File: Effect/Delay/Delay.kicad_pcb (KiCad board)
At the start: 2 copper layers, 32 x 75 mm, 23 parts, among them J1 Conn_01x04_Pin, J2 Conn_01x03_Pin, U1 PT2399

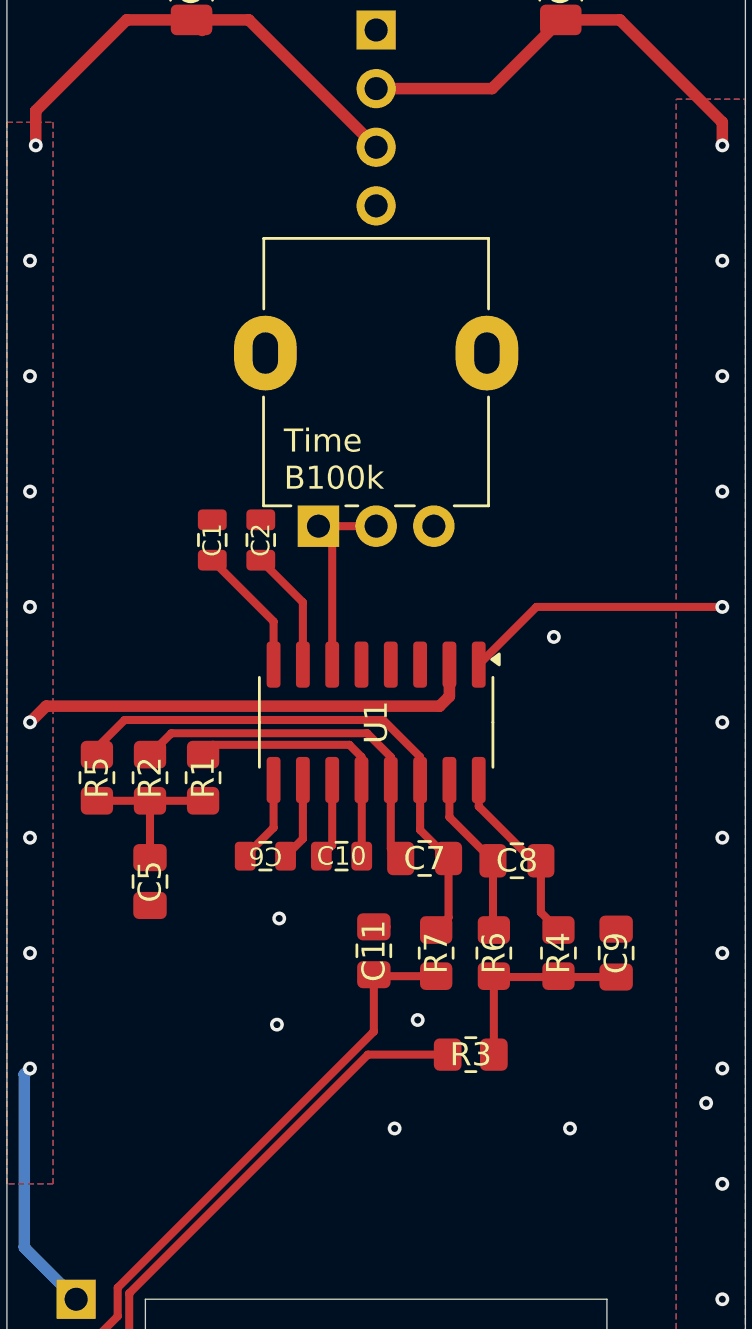
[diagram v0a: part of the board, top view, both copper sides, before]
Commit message: Do the manual ground stitching on delay board
Still don't have automated scripts, and I still like having something
that looks like ground stitching when prepping for fabrication.

Signed-off-by: Linus Torvalds <torvalds@linux-foundation.org>
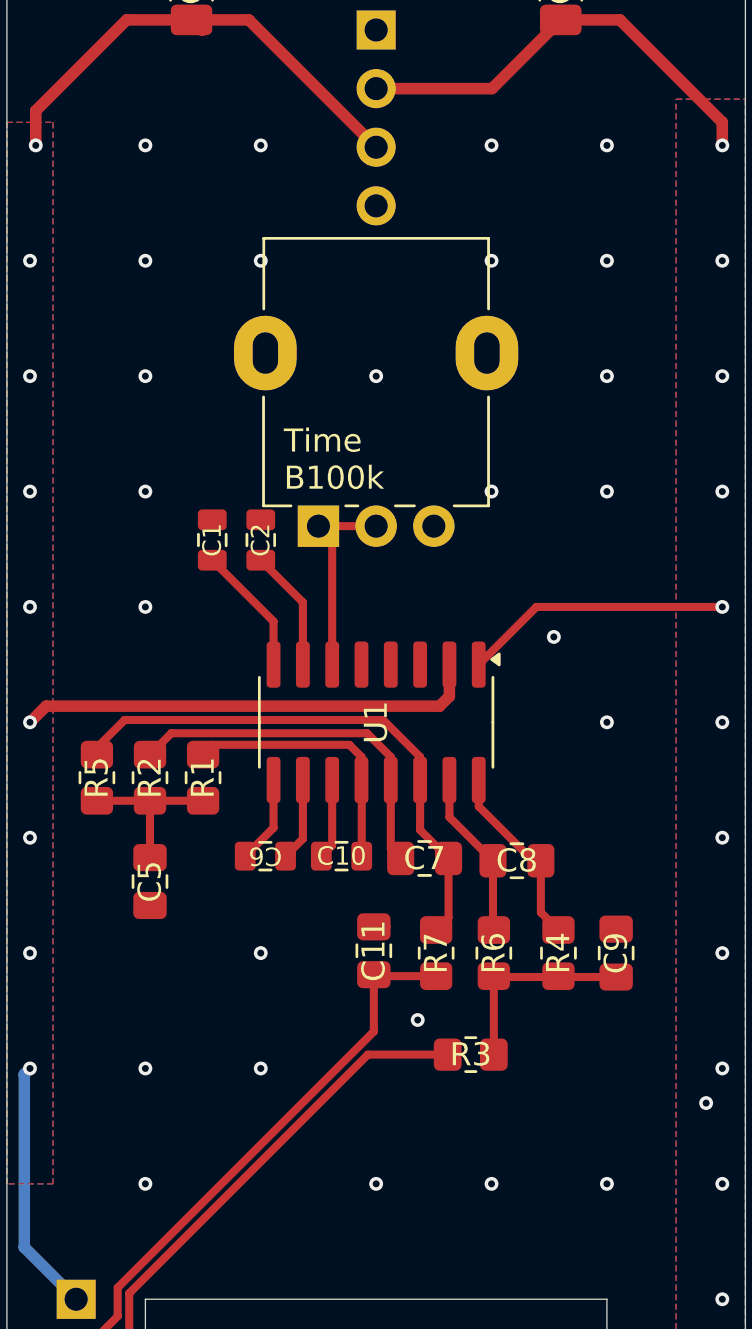
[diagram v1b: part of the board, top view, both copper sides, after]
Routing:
- net AGND: vias 11 -> 30
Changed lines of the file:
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@@
+	)
+	(via
+		(at 90 115)
+		(size 0.6)
+		(drill 0.3)
+		(layers "F.Cu" "B.Cu")
+		(free yes)
+		(net 2)
 	)
 	(via
@@
 	)
 	(via
-		(at 100.8 117.6)
+		(at 95 110)
+		(size 0.6)
+		(drill 0.3)
+		(layers "F.Cu" "B.Cu")
+		(free yes)
+		(net 2)
+	)
+	(via
+		(at 90 120)
 		(size 0.6)
 		(drill 0.3)
@@
 	)
 	(via
-		(at 95.7 113.1)
+		(at 90 75)
+		(size 0.6)
+		(drill 0.3)
+		(layers "F.Cu" "B.Cu")
+		(free yes)
+		(net 2)
+	)
+	(via
+		(at 90 90)
+		(size 0.6)
+		(drill 0.3)
+		(layers "F.Cu" "B.Cu")
+		(free yes)
+		(net 2)
+	)
+	(via
+		(at 110 120)
+		(size 0.6)
+		(drill 0.3)
+		(layers "F.Cu" "B.Cu")
+		(free yes)
+		(net 2)
+	)
+	(via
+		(at 110 100)
+		(size 0.6)
+		(drill 0.3)
+		(layers "F.Cu" "B.Cu")
+		(free yes)
+		(net 2)
+	)
+	(via
+		(at 95 75)
 		(size 0.6)
 		(drill 0.3)
@@
 	)
 	(via
+		(at 90 95)
+		(size 0.6)
+		(drill 0.3)
+		(layers "F.Cu" "B.Cu")
+		(free yes)
+		(net 2)
+	)
+	(via
 		(at 91.75 64.25)
 		(size 0.6)
@@
 	)
 	(via
+		(at 105 90)
+		(size 0.6)
+		(drill 0.3)
+		(layers "F.Cu" "B.Cu")
+		(free yes)
+		(net 2)
+	)
+	(via
+		(at 110 80)
+		(size 0.6)
+		(drill 0.3)
+		(layers "F.Cu" "B.Cu")
+		(free yes)
+		(net 2)
+	)
+	(via
 		(at 101.8 112.9)
 		(size 0.6)
@@
 	)
 	(via
-		(at 95.8 108.5)
+		(at 100 85)
+		(size 0.6)
+		(drill 0.3)
+		(layers "F.Cu" "B.Cu")
+		(free yes)
+		(net 2)
+	)
+	(via
+		(at 110 90)
+		(size 0.6)
+		(drill 0.3)
+		(layers "F.Cu" "B.Cu")
+		(free yes)
+		(net 2)
+	)
+	(via
+		(at 110 75)
+		(size 0.6)
+		(drill 0.3)
+		(layers "F.Cu" "B.Cu")
+		(free yes)
+		(net 2)
+	)
+	(via
+		(at 105 75)
 		(size 0.6)
 		(drill 0.3)
@@
 	)
 	(via
-		(at 108.4 117.6)
-		(size 0.6)
-		(drill 0.3)
+		(at 95 115)
+		(size 0.6)
+		(drill 0.3)
+		(layers "F.Cu" "B.Cu")
+		(free yes)
+		(net 2)
+	)
+	(via
+		(at 100 120)
+		(size 0.6)
+		(drill 0.3)
+		(layers "F.Cu" "B.Cu")
+		(free yes)
+		(net 2)
+	)
+	(via
+		(at 95 80)
+		(size 0.6)
+		(drill 0.3)
+		(layers "F.Cu" "B.Cu")
+		(free yes)
+		(net 2)
+	)
+	(via
+		(at 90 80)
+		(size 0.6)
+		(drill 0.3)
+		(layers "F.Cu" "B.Cu")
+		(free yes)
+		(net 2)
+	)
+	(via
+		(at 105 120)
+		(size 0.6)
+		(drill 0.3)
+		(layers "F.Cu" "B.Cu")
+		(free yes)
+		(net 2)
+	)
+	(via
+		(at 90 85)
+		(size 0.6)
+		(drill 0.3)
+		(layers "F.Cu" "B.Cu")
+		(free yes)
+		(net 2)
+	)
+	(via
+		(at 105 80)
+		(size 0.6)
+		(drill 0.3)
+		(layers "F.Cu" "B.Cu")
+		(free yes)
+		(net 2)
+	)
+	(via
+		(at 110 85)
+		(size 0.6)
+		(drill 0.3)

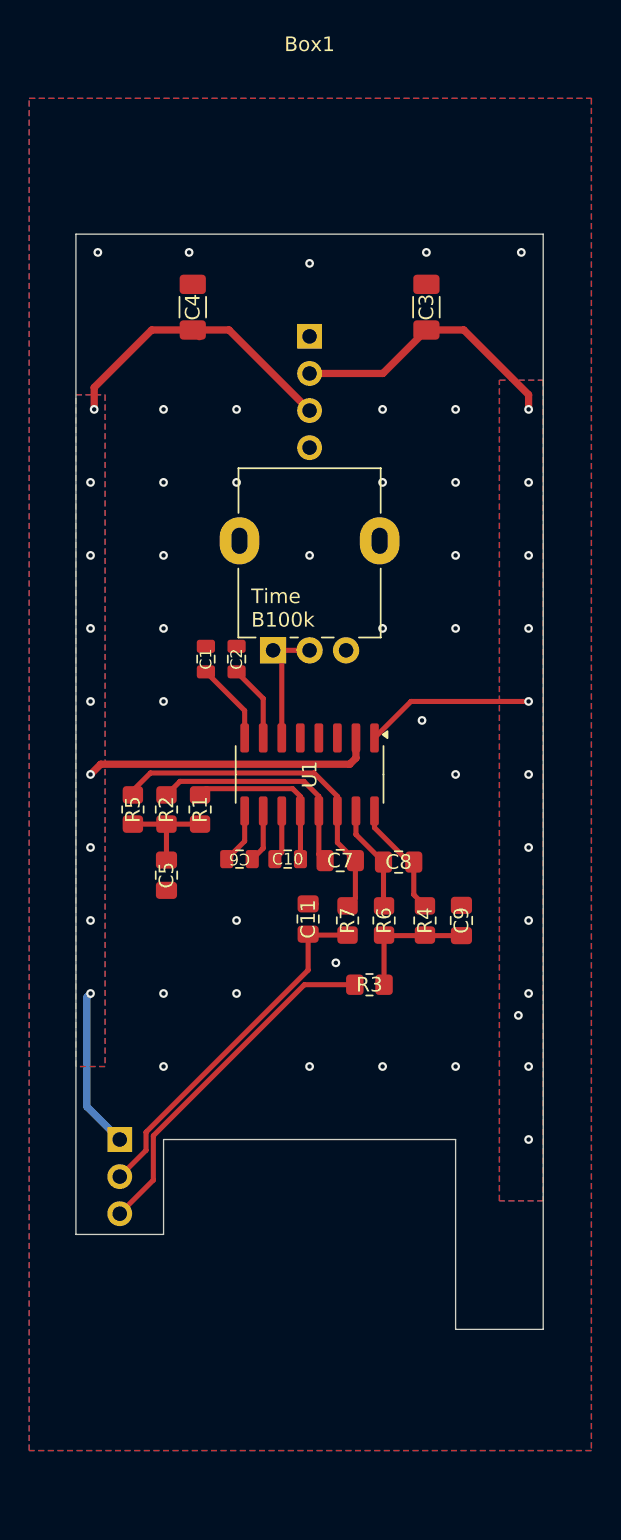
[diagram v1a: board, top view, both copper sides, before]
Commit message: Turn the delay pedal into an echo
For testing, the delay pedal did a pure delayed output.  And it tests
fine, but I think what is more interesting to use is an actual echo
pedal where the delay gets fed back into the input.

Maybe it could have a mixed mode and do either? Or both? Anyway, this
just does the feedback thing.

Signed-off-by: Linus Torvalds <torvalds@linux-foundation.org>
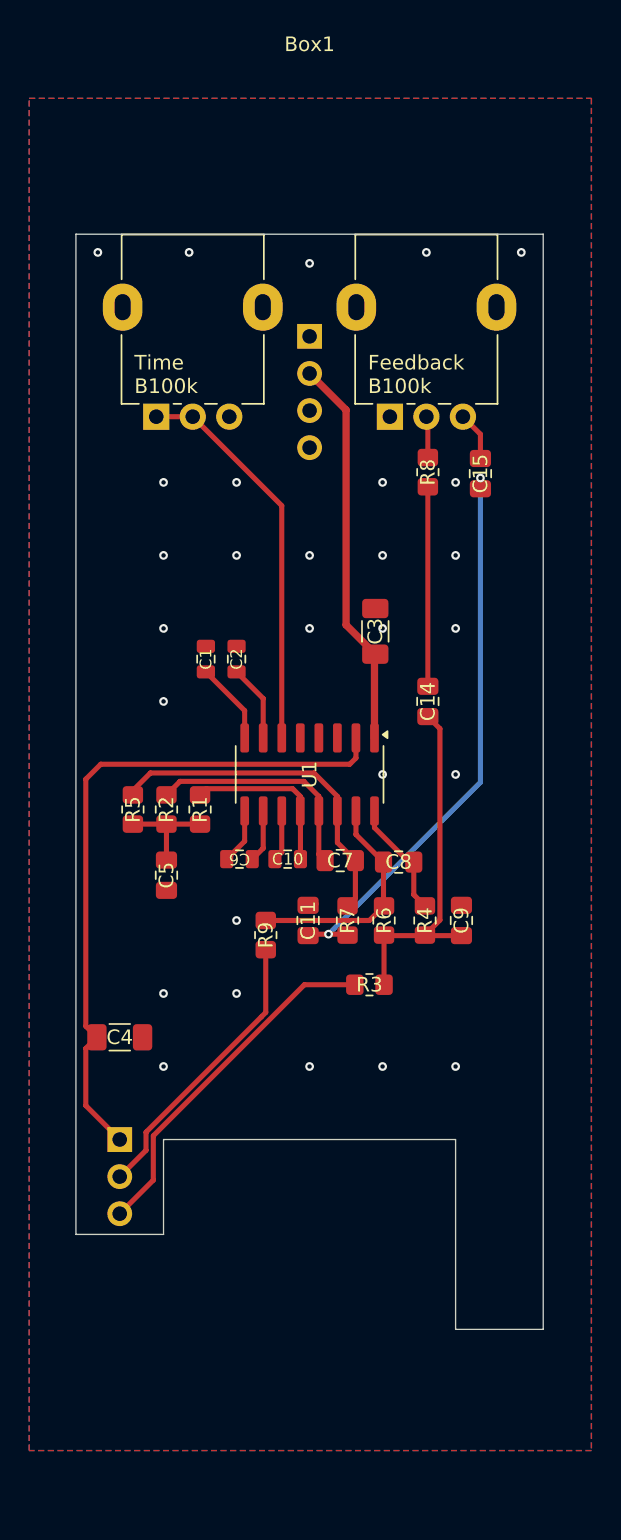
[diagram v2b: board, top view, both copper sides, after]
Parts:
- added C14: 4.7uF, Capacitor_SMD:C_0805_2012Metric_Pad1.18x1.45mm_HandSolder, F.Cu at (108.1, 95.0)
- added C15: 10uF, Capacitor_SMD:C_0805_2012Metric_Pad1.18x1.45mm_HandSolder, F.Cu at (111.7, 79.4)
- added R8: 10k, Resistor_SMD:R_0805_2012Metric_Pad1.20x1.40mm_HandSolder, F.Cu at (108.1, 79.3)
- added R9: 10k, Resistor_SMD:R_0805_2012Metric_Pad1.20x1.40mm_HandSolder, F.Cu at (97.0, 111.0)
- added RV4: B50k Feedback, Mylib:Potentiometer_9mm_MP, F.Cu at (108.0, 68.0)
- R7: value 2k7 -> 5.6k
- moved C4 50.2 mm to (87.0, 118.0), turned to 0 degrees
- moved C3 22.5 mm to (104.5, 90.2)
- moved RV1 17.9 mm to (92.0, 68.0)
- moved C11 0.10 mm to (99.9, 110.0)
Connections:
- net AGND renamed GND
- C11 pad 2: OUT -> DELAY
- J1 pad 3: VREF -> unconnected-(J1-Pin_3-Pad3)
- R7 pad 2: OUT -> DELAY
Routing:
- net DELAY: track 0.00 -> 39.1 mm, vias 0 -> 2
- net VCO: track 8.75 -> 27.0 mm
- net Net-(C14-Pad2): track 8.72 -> 24.4 mm
- net Net-(C14-Pad1): track 0.00 -> 13.7 mm
- net LPF1-OUT: track 7.30 -> 15.8 mm
- net VREF: track 51.9 -> 46.7 mm, vias 9 -> 0
- net OUT: track 24.7 -> 19.7 mm
- net +5V: track 30.7 -> 26.8 mm, vias 12 -> 0
- net Net-(C15-Pad2): track 0.00 -> 3.36 mm
- net Net-(R8-Pad2): track 0.00 -> 2.84 mm
- net GND: track 0.56 -> 0.60 mm, vias 30 -> 28
- removed copper zone on B.Cu, net +5V
- removed copper zone on F.Cu, net +5V
- removed copper zone on B.Cu, net VREF
- removed copper zone on F.Cu, net VREF
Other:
- board text added: "Feedback B100k"
